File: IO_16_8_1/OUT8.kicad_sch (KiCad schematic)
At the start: 44 parts, among them J10 Conn_01x06, J11 Conn_01x06, J9 Conn_01x06, Q25 IRLR3410, Q26 IRLR3410, Q27 IRLR3410, Q28 IRLR3410, Q29 IRLR3410, Q30 IRLR3410, Q31 IRLR3410, Q32 IRLR3410

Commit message: Release 1.1.0
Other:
- title: High Power Outputs -> IO_16_8_1
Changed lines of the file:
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@@
   (paper "A3")
   (title_block
-    (title "High Power Outputs")
-    (date "2023-01-29")
-    (rev "1.0.0")
+    (title "IO_16_8_1")
+    (date "2024-10-04")
+    (rev "1.1.0")
   )
   (junction (at 184.15 130.81) (diameter 0) (color 0 0 0 0)

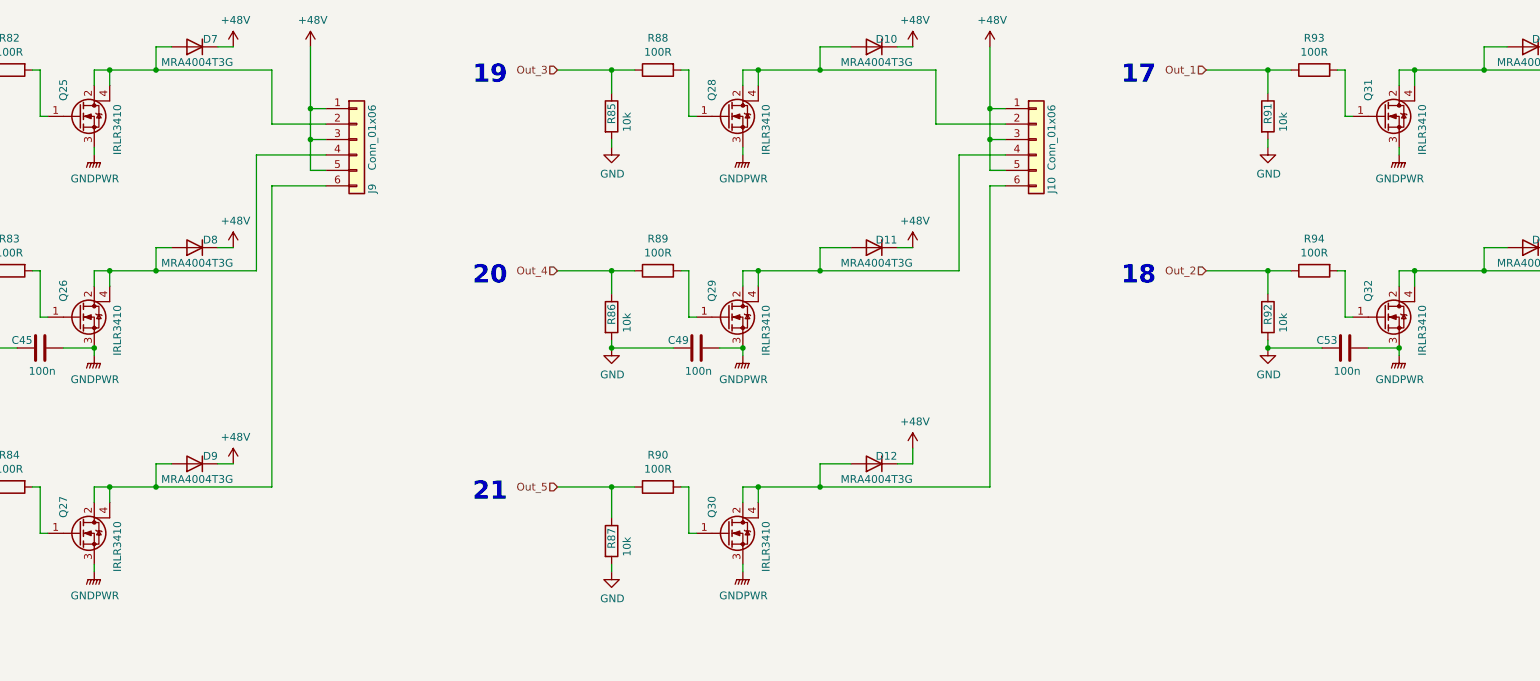
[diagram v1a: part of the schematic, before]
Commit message: changed MOSFETs
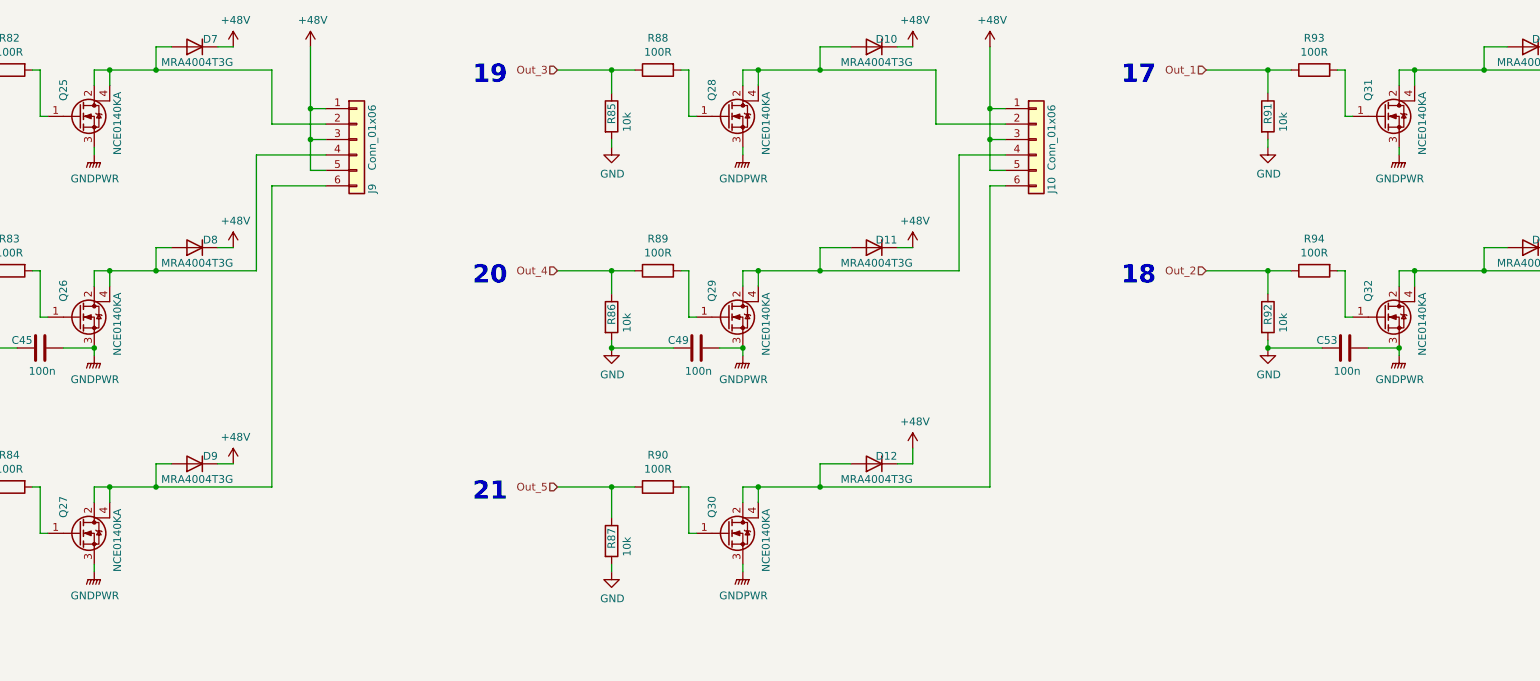
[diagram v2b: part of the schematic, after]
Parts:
- Q25, Q26, Q27, Q28, Q29, Q30, Q31, Q32: value IRLR3410 -> NCE0140KA
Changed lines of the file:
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@@
   (title_block
     (title "IO_16_8_1")
-    (date "2024-10-04")
-    (rev "1.1.0")
+    (date "2024-11-16")
+    (rev "1.1.1")
   )
   (junction (at 184.15 130.81) (diameter 0) (color 0 0 0 0)
@@
       (effects (font (size 1.27 1.27)) (justify left))
     )
-    (property "Value" "IRLR3410" (id 1) (at 295.91 132.08 90)
+    (property "Value" "NCE0140KA" (id 1) (at 295.91 132.08 90)
       (effects (font (size 1.27 1.27)) (justify left))
     )
@@
       (effects (font (size 1.27 1.27)) (justify left))
     )
-    (property "Value" "IRLR3410" (id 1) (at 187.96 167.64 90)
+    (property "Value" "NCE0140KA" (id 1) (at 187.96 167.64 90)
       (effects (font (size 1.27 1.27)) (justify left))
     )
@@
       (effects (font (size 1.27 1.27)) (justify left))
     )
-    (property "Value" "IRLR3410" (id 1) (at 187.96 132.08 90)
+    (property "Value" "NCE0140KA" (id 1) (at 187.96 132.08 90)
       (effects (font (size 1.27 1.27)) (justify left))
     )
@@
       (effects (font (size 1.27 1.27)) (justify left))
     )
-    (property "Value" "IRLR3410" (id 1) (at 81.28 99.06 90)
+    (property "Value" "NCE0140KA" (id 1) (at 81.28 99.06 90)
       (effects (font (size 1.27 1.27)) (justify left))
     )
@@
       (effects (font (size 1.27 1.27)) (justify left))
     )
-    (property "Value" "IRLR3410" (id 1) (at 81.28 167.64 90)
+    (property "Value" "NCE0140KA" (id 1) (at 81.28 167.64 90)
       (effects (font (size 1.27 1.27)) (justify left))
     )
@@
       (effects (font (size 1.27 1.27)) (justify left))
     )
-    (property "Value" "IRLR3410" (id 1) (at 81.28 132.08 90)
+    (property "Value" "NCE0140KA" (id 1) (at 81.28 132.08 90)
       (effects (font (size 1.27 1.27)) (justify left))
     )
@@
       (effects (font (size 1.27 1.27)) (justify left))
     )
-    (property "Value" "IRLR3410" (id 1) (at 295.91 99.06 90)
+    (property "Value" "NCE0140KA" (id 1) (at 295.91 99.06 90)
       (effects (font (size 1.27 1.27)) (justify left))
     )
@@
       (effects (font (size 1.27 1.27)) (justify left))
     )
-    (property "Value" "IRLR3410" (id 1) (at 187.96 99.06 90)
-      (effects (font (size 1.27 1.27)) (justify left))
-    )
+    (property "Value" "NCE0140KA" (id 1) (at 187.96 99.06 90)
+      (effects (font (size 1.27 1.27)) (justify left))
+    )
